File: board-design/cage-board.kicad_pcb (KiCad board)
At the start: 2 copper layers, 127 x 127 mm, 34 parts, among them J1 Jack-DC, J10 73131-0240, J11 73131-0240, J12 73131-0240, J13 Conn_01x02, J14 Conn_01x02, J15 Conn_02x13_test_points, J2 Conn_02x17_Ribbon, J3 TB002-500-03BE, J4 73131-0240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

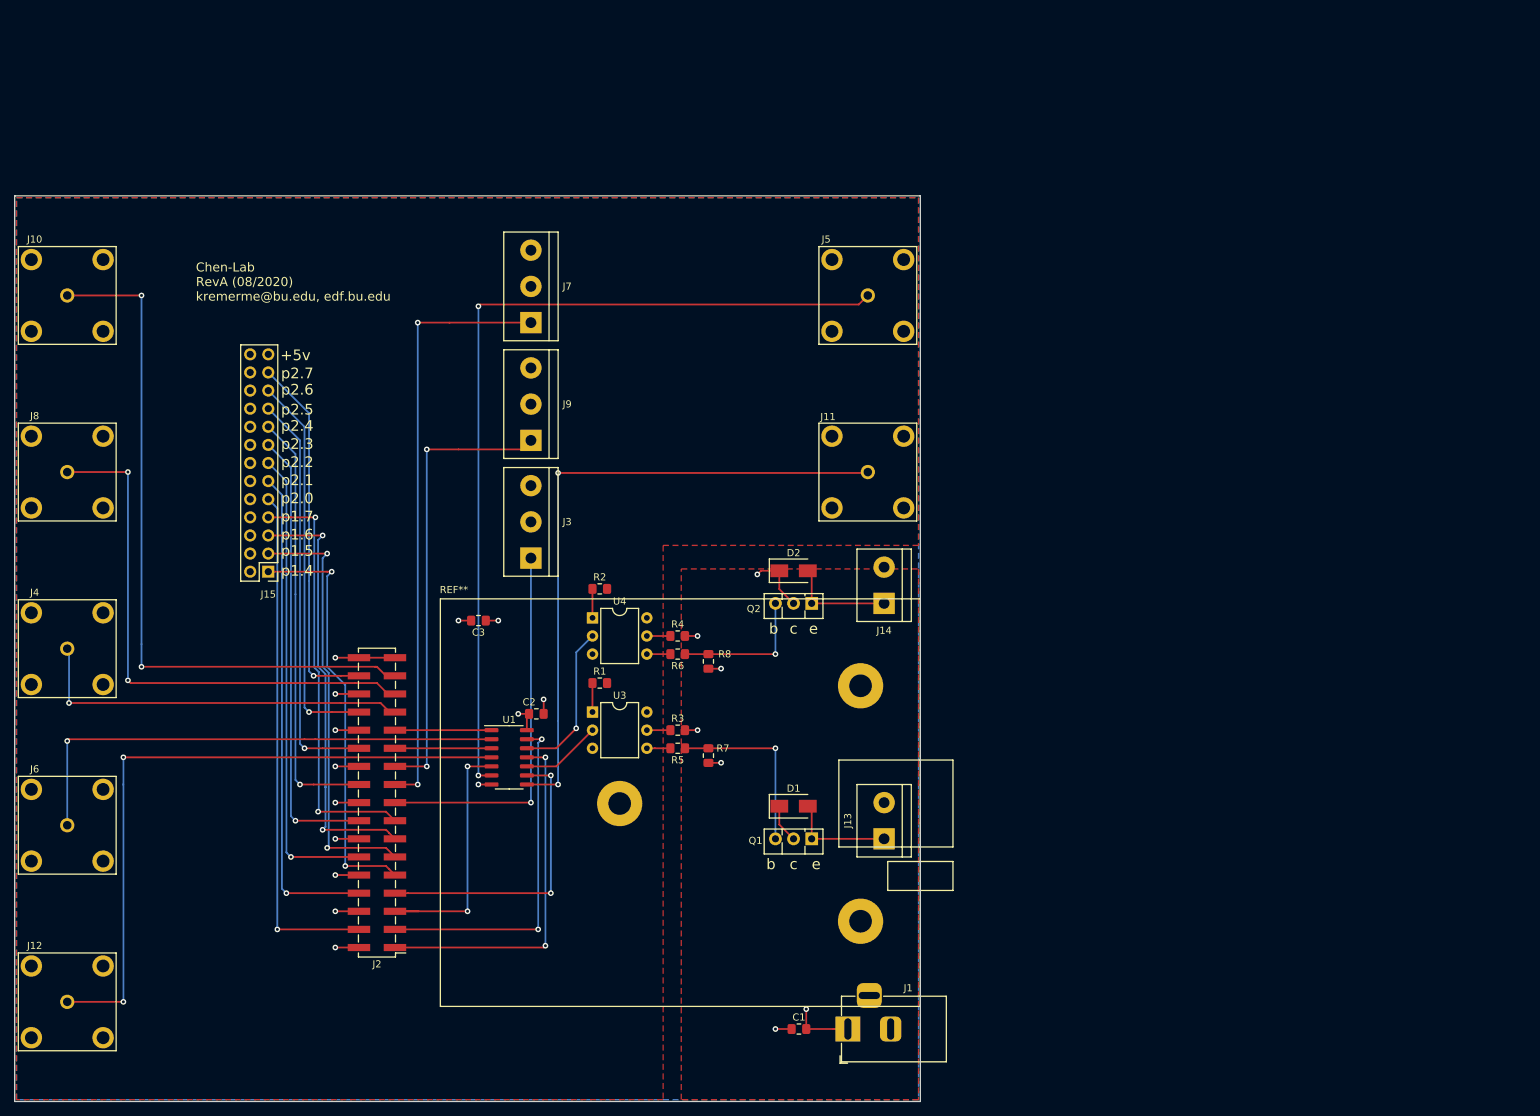
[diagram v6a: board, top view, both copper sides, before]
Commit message: added inch to board length and spaced out connectors more
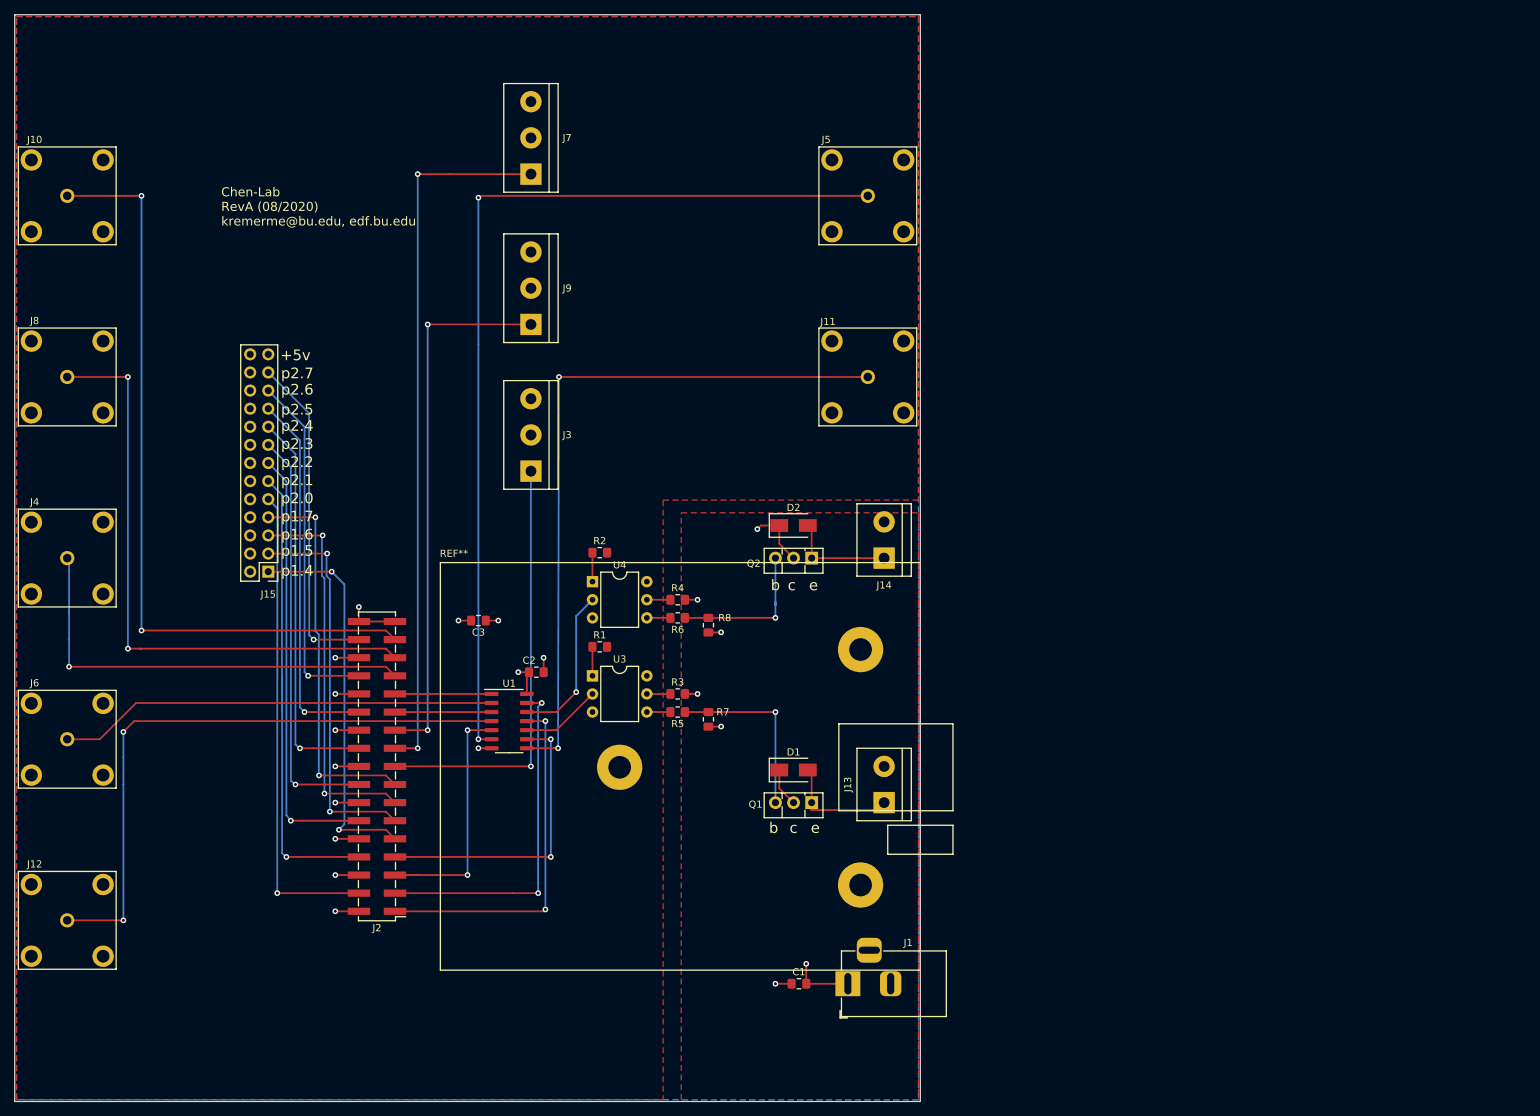
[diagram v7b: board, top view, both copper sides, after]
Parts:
- moved J7 20.8 mm to (148.6, 22.4)
- moved J9 16.3 mm to (148.6, 43.4)
- moved J10 14.0 mm to (83.6, 25.4)
- moved J5 14.0 mm to (195.8, 25.4)
- moved J11 13.3 mm to (195.8, 50.8)
- moved J8 13.3 mm to (83.6, 50.8)
- moved J4 12.7 mm to (83.6, 76.2)
- moved J3 12.2 mm to (148.6, 64.0)
- moved J6 12.1 mm to (83.6, 101.6)
- moved J12 11.4 mm to (83.6, 127.0)
- moved C1 6.35 mm to (186.2, 135.9)
- moved J1 6.35 mm to (193.0, 135.9)
- moved D2 6.35 mm to (185.4, 71.6)
- moved J14 6.35 mm to (198.1, 76.2)
- moved Q2 6.35 mm to (188.0, 76.2)
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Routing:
- net /P0.1: track 83.8 -> 99.6 mm
- net /P0.2: track 64.0 -> 76.3 mm
- net Net-(J5-Pad1): track 122.9 -> 132.5 mm
- net Net-(J6-Pad1): track 71.4 -> 62.0 mm, vias 1 -> 0
- net /P0.6: track 76.0 -> 85.2 mm
- net /P0.5: track 54.0 -> 63.1 mm
- net /P0.7: track 98.6 -> 107.5 mm
- net Net-(J11-Pad1): track 91.6 -> 99.9 mm
- net Net-(J12-Pad1): track 93.8 -> 86.7 mm
- net /P0.0: track 53.4 -> 60.5 mm
- net /P1.6: track 60.6 -> 54.4 mm
- net /P1.5: track 60.3 -> 54.3 mm
- net /P1.7: track 59.3 -> 54.0 mm
- net /P2.6: track 54.5 -> 49.3 mm
- net /P2.2: track 66.1 -> 61.0 mm
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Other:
- board size 127 x 127 mm -> 127 x 152.4 mm

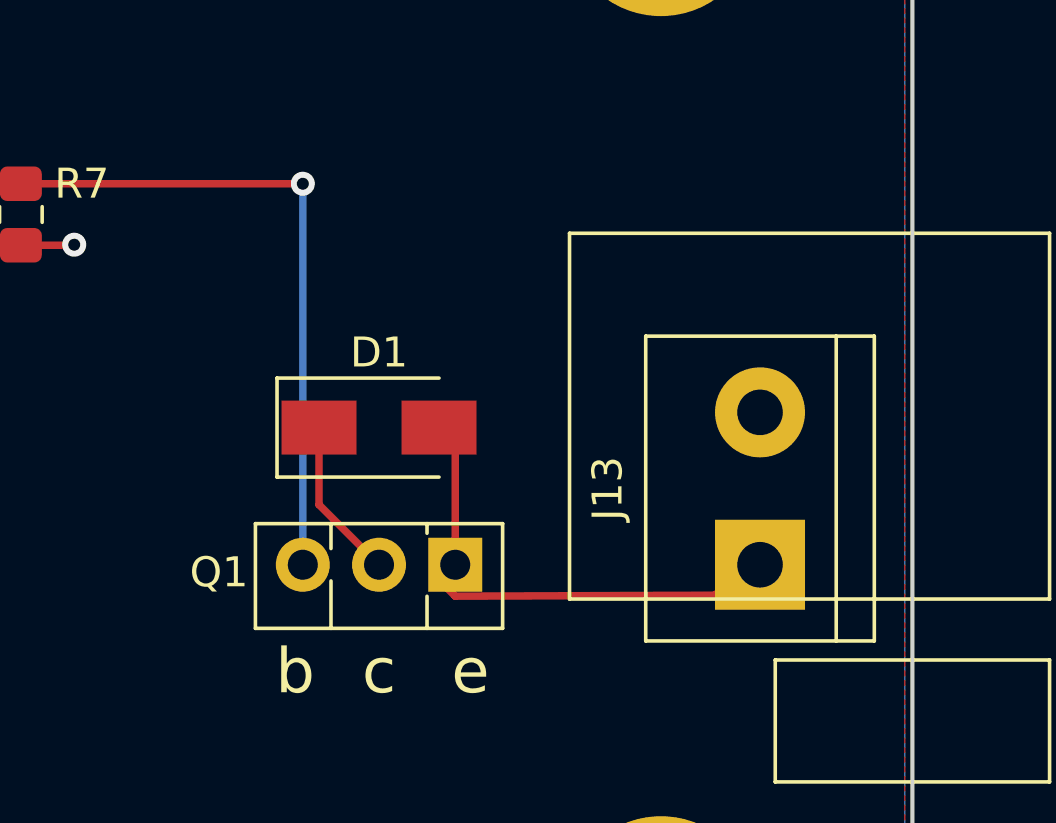
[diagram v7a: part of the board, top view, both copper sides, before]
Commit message: adding dimensions for protocase
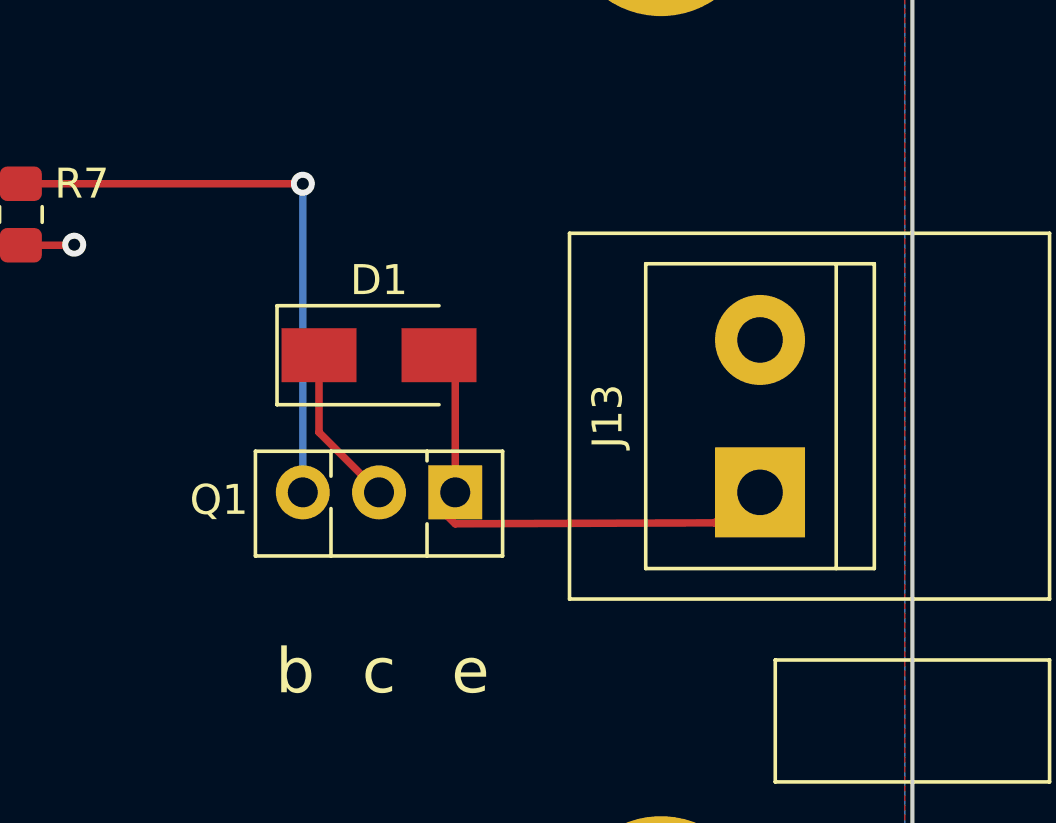
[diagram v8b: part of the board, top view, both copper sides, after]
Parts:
- moved D1 2.41 mm to (185.4, 103.5)
- moved J13 2.41 mm to (198.1, 108.1)
- moved Q1 2.41 mm to (188.0, 108.1)
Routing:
- net Net-(Q1-Pad3): track 25.4 -> 23.0 mm
